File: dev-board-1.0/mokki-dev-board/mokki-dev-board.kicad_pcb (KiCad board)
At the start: 2 copper layers, 43 parts, among them J1 USB_B_Micro, J2 SWD connector, J3 OLED_Connector, J4 BLE_Connector, J5 DEBUG_Conn, J6 User port, Q1 BC847B, SW1 SW_PWR, SW10 BTN_B, SW2 BTN_RST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

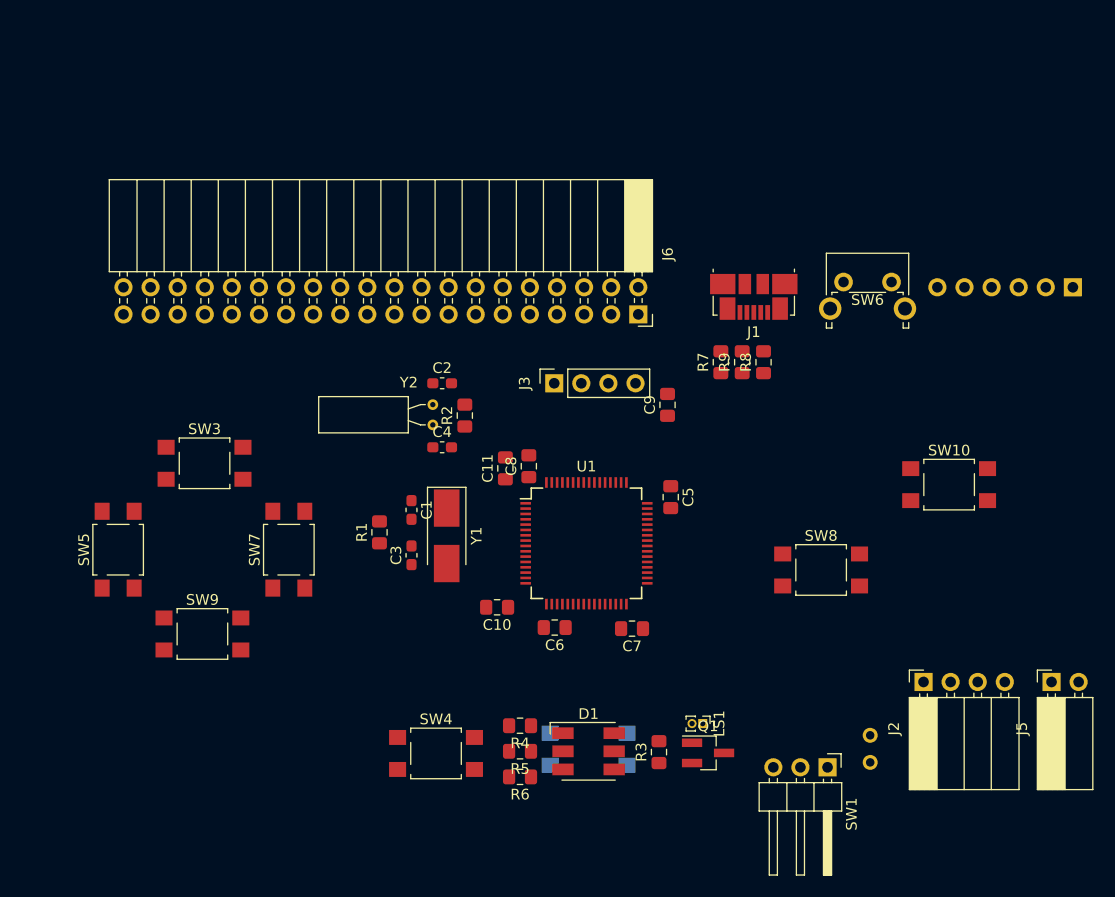
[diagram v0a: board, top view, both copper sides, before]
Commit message: Made some space for connections
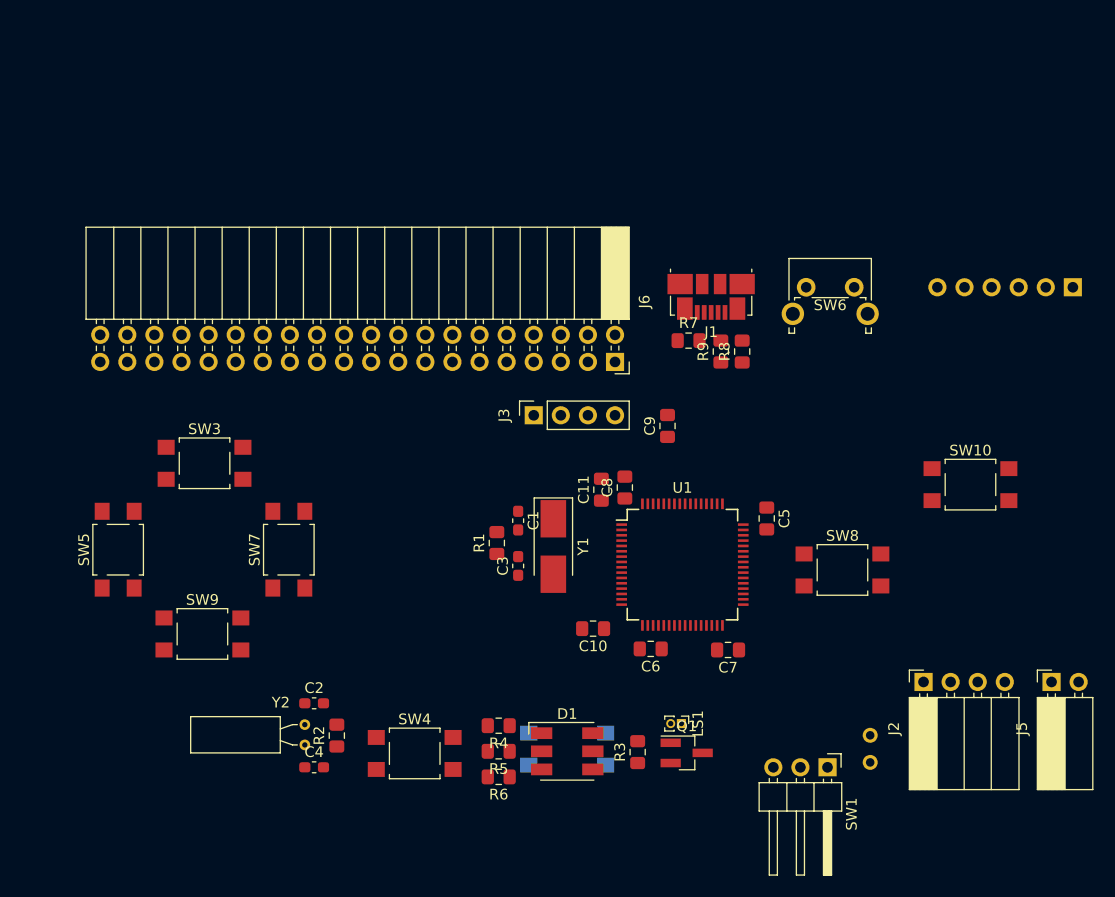
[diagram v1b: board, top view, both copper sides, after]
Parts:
- moved C2 32.3 mm to (125.9, 141.0)
- moved C4 32.3 mm to (125.9, 147.0)
- moved R2 32.3 mm to (128.0, 144.0)
- moved Y2 32.3 mm to (125.0, 143.0)
- moved R1 11.0 mm to (143.0, 126.0)
- moved C1 10.0 mm to (145.0, 123.9)
- moved C3 10.0 mm to (145.0, 128.1)
- moved Y1 10.0 mm to (148.3, 126.3)
- moved C10 9.22 mm to (152.0, 134.0)
- moved C11 9.22 mm to (152.8, 121.0)
- moved C5 9.22 mm to (168.3, 123.7)
- moved C6 9.22 mm to (157.4, 135.9)
- moved C7 9.22 mm to (164.7, 136.0)
- moved C8 9.22 mm to (155.0, 120.8)
- moved U1 9.22 mm to (160.4, 128.0)
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
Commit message: Modified some footprints, used 0603 capacitors
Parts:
- C10, C11, C5, C6, C7, C8: footprint Capacitor_SMD:C_0805_2012Metric_Pad1.15x1.40mm_HandSolder -> Capacitor_SMD:C_0603_1608Metric_Pad1.05x0.95mm_HandSolder
- LS1: footprint Connector_PinHeader_1.00mm:PinHeader_1x02_P1.00mm_Vertical -> TestPoint:tp-smd-2pad
- R1, R2: footprint Resistor_SMD:R_0805_2012Metric_Pad1.15x1.40mm_HandSolder -> Resistor_SMD:R_0603_1608Metric_Pad1.05x0.95mm_HandSolder
- moved LS1 0.95 mm to (160.0, 142.0), turned to 180 degrees
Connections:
- J1 pad 1: Net-(J1-Pad1) -> (no net)
- J1 pad 4: Net-(J1-Pad4) -> (no net)
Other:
- net class Default: via_dia 0.8 -> 0.7; via_drill 0.4 -> 0.3

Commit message: Final placement (?)
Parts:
- moved SW9 21.9 mm to (115.5, 112.6)
- moved SW7 21.6 mm to (123.1, 105.0)
- moved SW5 21.6 mm to (107.9, 105.0)
- moved SW3 21.1 mm to (115.5, 97.4)
- moved SW10 20.6 mm to (186.6, 99.9)
- moved U1 20.5 mm to (158.7, 107.5)
- moved J3 20.5 mm to (144.7, 93.6)
- moved SW1 20.4 mm to (171.4, 126.7)
- moved J1 20.4 mm to (160.8, 82.7)
- moved J5 20.4 mm to (192.9, 118.7)
- moved C3 20.3 mm to (143.4, 107.9)
- moved C10 20.3 mm to (150.5, 113.7)
- moved C2 20.3 mm to (124.4, 120.7)
- moved C4 20.3 mm to (124.4, 126.7)
- moved C6 20.3 mm to (155.9, 115.6)
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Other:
- board outline added: 100 x 50 mm

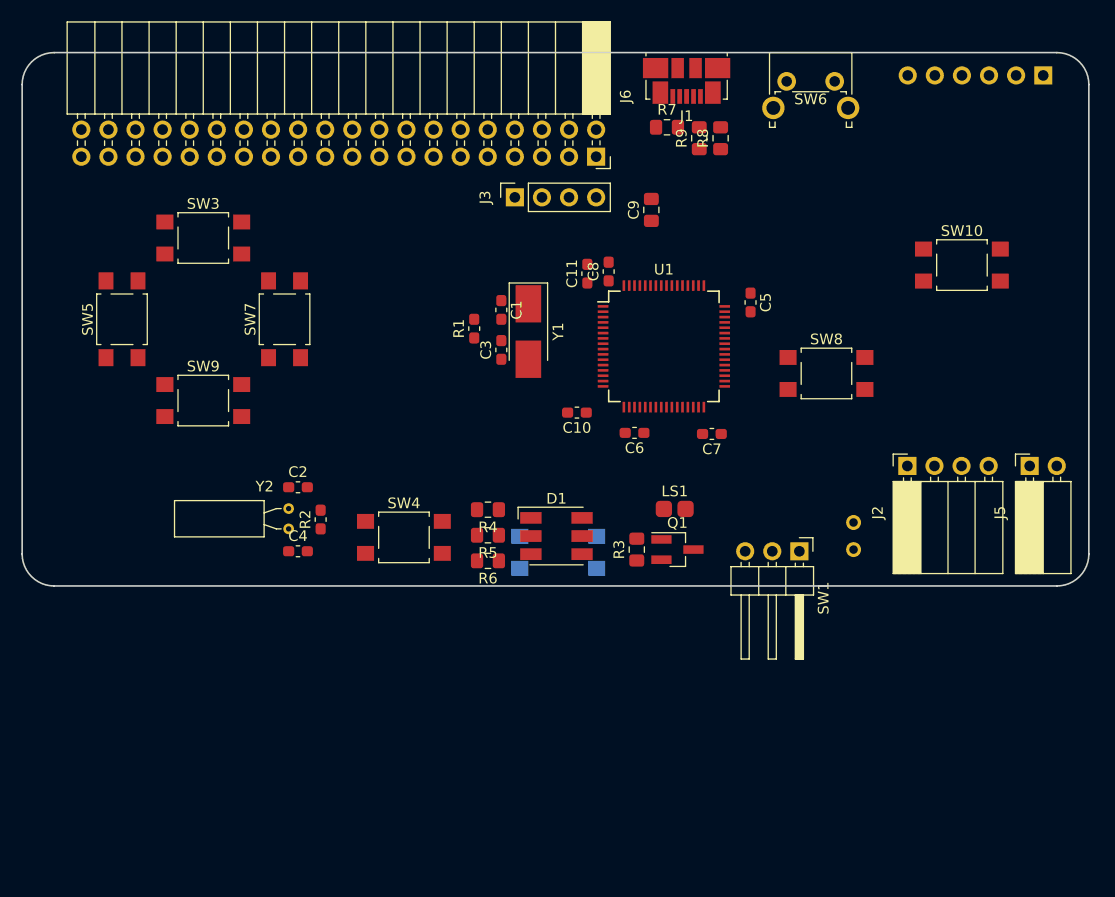
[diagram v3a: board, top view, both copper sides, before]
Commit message: Silkscreen, buttons placement
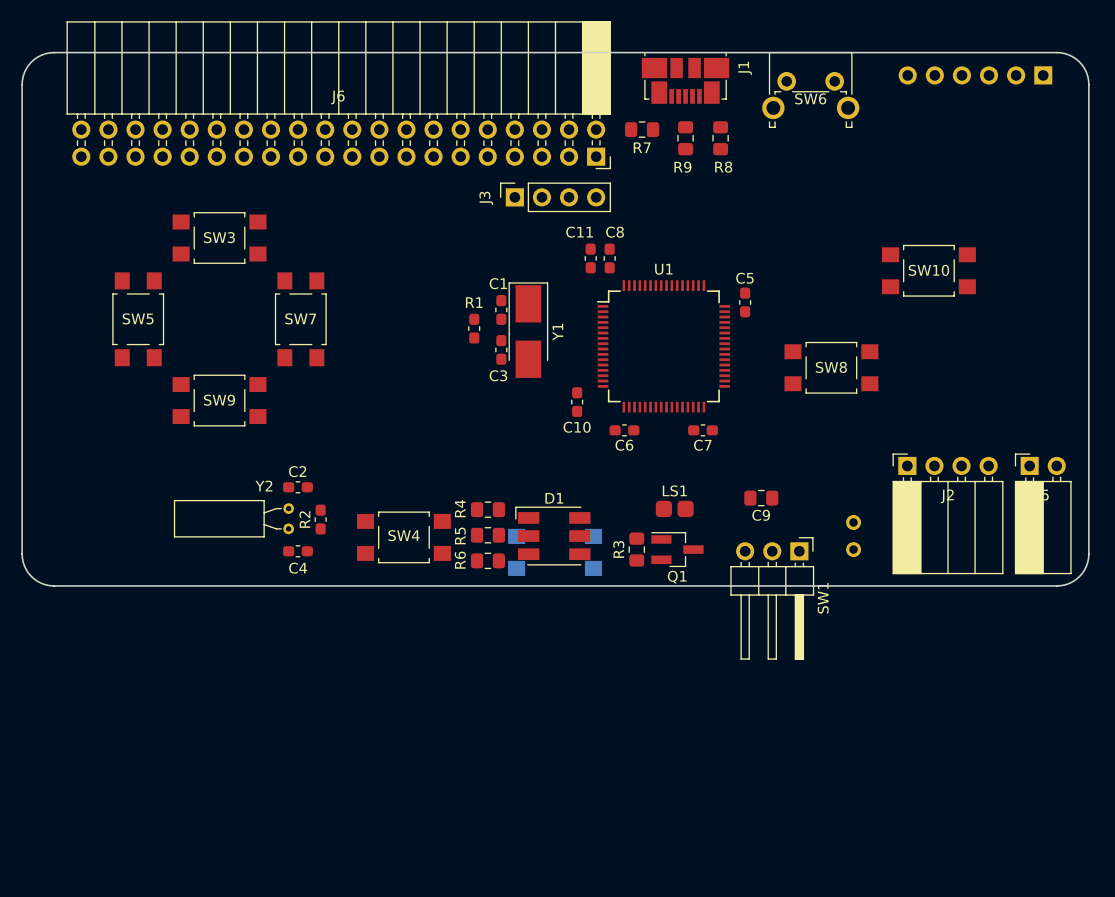
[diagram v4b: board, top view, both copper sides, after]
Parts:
- moved C9 28.9 mm to (167.8, 121.8), turned to 180 degrees
- moved SW10 3.14 mm to (183.5, 100.5)
- moved R7 2.34 mm to (156.6, 87.2)
- moved SW3 1.52 mm to (117.0, 97.4)
- moved SW5 1.52 mm to (109.4, 105.0)
- moved SW7 1.52 mm to (124.6, 105.0)
- moved SW9 1.52 mm to (117.0, 112.6)
- moved C11 1.46 mm to (151.8, 99.3)
- moved R9 1.28 mm to (160.7, 88.0)
- moved C8 1.23 mm to (153.6, 99.3)
- moved C10 0.99 mm to (150.5, 112.8), turned to 90 degrees
- moved C6 0.97 mm to (155.0, 115.4)
- moved C7 0.90 mm to (162.3, 115.4)
- moved SW8 0.71 mm to (174.4, 109.5)
- moved C5 0.50 mm to (166.3, 103.4)
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- renumbered SW2 to RESET
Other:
- board text added: "+"
- board text added: "-"

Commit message: PCB design finished
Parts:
- removed RESET: BTN_RST, Button_Switch_SMD:SW_SPST_TL3305B
- added SW2: BTN_RST, Button_Switch_SMD:SW_SPST_TL3305B, B.Cu at (148.5, 126.8)
- BT1: footprint TestPoint:TestPoint_2Pads_Pitch2.54mm_Drill0.8mm -> Connector_PinHeader_2.54mm:PinHeader_1x02_P2.54mm_Vertical
- J4: moved to F.Cu
- moved J4 13.0 mm to (181.3, 82.1)
- moved R2 12.8 mm to (113.7, 123.4), turned to 270 degrees
- moved C4 10.6 mm to (115.9, 120.4), turned to 180 degrees
- moved C2 10.2 mm to (115.9, 126.4), turned to 180 degrees
- moved C11 7.49 mm to (150.3, 106.6), turned to 270 degrees
- moved Y2 6.96 mm to (116.7, 124.4), turned to 90 degrees
- moved C10 3.06 mm to (150.3, 109.7)
- moved R8 1.76 mm to (162.2, 88.0)
- moved R7 1.69 mm to (158.1, 88.0), turned to 90 degrees
- moved SW4 1.50 mm to (132.8, 125.3)
- moved C8 1.16 mm to (154.3, 100.2), turned to 0 degrees
- moved C5 1.13 mm to (165.4, 102.7), turned to 0 degrees
- moved C9 0.51 mm to (167.8, 122.3)
- moved R9 0.51 mm to (160.2, 88.0)
- moved C7 0.51 mm to (162.3, 114.9)
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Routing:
- net GND: track 0.00 -> 102.8 mm, vias 0 -> 22
- net VCC: track 0.00 -> 70.9 mm, vias 0 -> 9
- net /NRST: track 0.00 -> 67.8 mm, vias 0 -> 2
- net /GPIO_PC4_A: track 0.00 -> 66.6 mm, vias 0 -> 1
- net /GPIO_PB0_AT: track 0.00 -> 66.4 mm, vias 0 -> 1
- net /GPIO_PB1_AT: track 0.00 -> 64.9 mm
- net /GPIO_PC5_A: track 0.00 -> 64.9 mm
- net /GPIO_PA1_AT: track 0.00 -> 63.9 mm, vias 0 -> 2
- net /GPIO_PC3_A: track 0.00 -> 63.3 mm, vias 0 -> 1
- net /USART5_TX: track 0.00 -> 57.0 mm, vias 0 -> 2
- net Net-(C2-Pad1): track 0.00 -> 55.9 mm, vias 0 -> 1
- net /GPIO_PC7_T: track 0.00 -> 55.1 mm, vias 0 -> 1
- net Net-(C4-Pad1): track 0.00 -> 53.7 mm, vias 0 -> 1
- net /GPIO_PC6_T: track 0.00 -> 53.2 mm, vias 0 -> 1
- net /GPIO_PC9_T: track 0.00 -> 52.1 mm, vias 0 -> 1
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- added copper zone on B.Cu, net GND
- added copper zone on F.Cu, net VCC
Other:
- net class power added: clearance 0.2, trace_width 0.35, via_dia 0.7, via_drill 0.3
- rule trace_min: 0.2 -> 0.19
- board text added: "RESET"

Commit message: board ready to production
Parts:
- J4: footprint Connector_PinSocket_2.54mm:PinSocket_1x06_P2.54mm_Horizontal -> Connector_PinSocket_2.54mm:PinSocket_1x06_P2.54mm_Vertical
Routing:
- net GND: track 102.8 -> 89.0 mm, vias 22 -> 21
- net Net-(J1-Pad6): track 10.8 -> 0.00 mm
- net /NRST: track 67.8 -> 65.9 mm
- net /GPIO_PB2: track 35.7 -> 34.6 mm
- net /USB_DM: track 25.4 -> 26.1 mm

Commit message: Final touches
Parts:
- added REF**: OSHW-Logo2_14.6x12mm_Copper, Symbol:OSHW-Logo2_14.6x12mm_Copper, B.Cu at (107.4, 114.4)
- added REF**: MountingHole_3.2mm_M3_DIN965, MountingHole:MountingHole_3.2mm_M3_DIN965, B.Cu at (102.8, 125.8)
- J4, SW1: moved to B.Cu
- moved SW2 0.28 mm to (148.5, 127.1)
- turned J4 to 270 degrees
- turned SW1 to 90 degrees
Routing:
- net GND: track 89.0 -> 89.7 mm
- net /GPIO_PA8: track 31.8 -> 31.3 mm
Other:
- board text added: "30-07-2018"
- board text added: "A"
- board text added: "B"
- board text added: "CLK"
- board text added: "Designed in Poland"
- board text added: "GND"
- board text added: "IO"
- board text added: "Mokki Dev Board v. 1.0"
- board text added: "NRST"
- board text added: "OFF"
- board text added: "ON"
- board text added: "R1"
- board text added: "Start"
- board text added: "TX"
- board text added: "www.mokki.org"

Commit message: Final version
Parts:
- Y2: footprint Crystal:Crystal_C38-LF_D3.0mm_L8.0mm_Horizontal -> Crystal:Crystal_C38-LF_D3.0mm_L8.0mm_Horizontal-no-drawing
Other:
- board text removed: "Designed in Poland"
